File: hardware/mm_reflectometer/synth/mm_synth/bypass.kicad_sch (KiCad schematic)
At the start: 5 parts

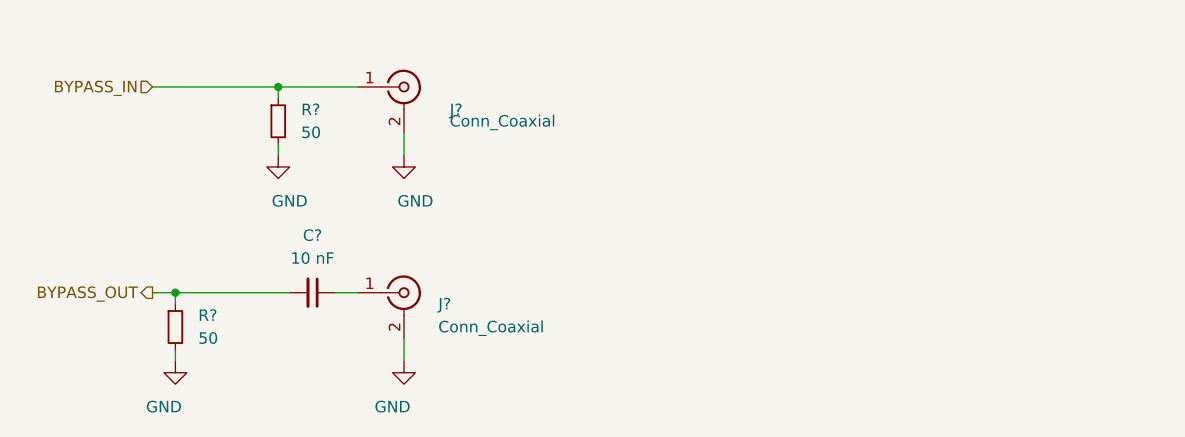
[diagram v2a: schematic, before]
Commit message: work on mm synth schematic - control signals and footprint assignments
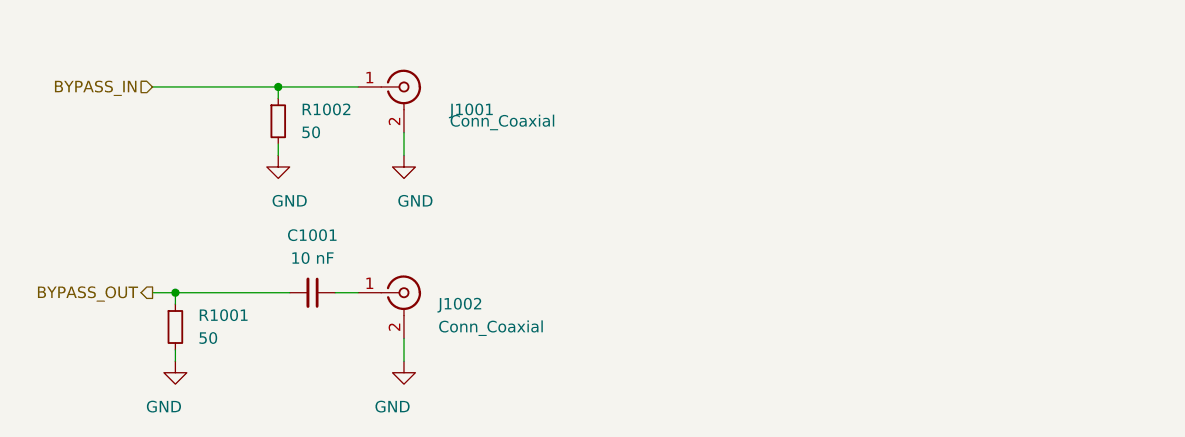
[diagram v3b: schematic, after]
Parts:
- C1001: renamed from C?; footprint (none) -> Capacitor_SMD:C_0402_1005Metric
- J1001, J1002: renamed from J?; footprint (none) -> jtk_rf_footprints:sw_edge_oshpark_4layer
- R1001, R1002: renamed from R?; footprint (none) -> Resistor_SMD:R_0402_1005Metric
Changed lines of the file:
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@@
-(kicad_sch (version 20210406) (generator eeschema)
+(kicad_sch (version 20210621) (generator eeschema)
   (paper "A4")
   (junction (at 110.49 114.3) (diameter 0.9144) (color 0 0 0 0))
@@
   (symbol (lib_id "power:GND") (at 110.49 121.92 0) (mirror y) (unit 1)
     (in_bom yes) (on_board yes)
-    (property "Reference" "#PWR0276" (id 0) (at 110.49 128.27 0)
+    (property "Reference" "#PWR01001" (id 0) (at 110.49 128.27 0)
       (effects (font (size 1.27 1.27)) hide)
     )
@@
   (symbol (lib_id "power:GND") (at 121.92 99.06 0) (unit 1)
     (in_bom yes) (on_board yes)
-    (property "Reference" "#PWR0277" (id 0) (at 121.92 105.41 0)
+    (property "Reference" "#PWR01002" (id 0) (at 121.92 105.41 0)
       (effects (font (size 1.27 1.27)) hide)
     )
@@
   (symbol (lib_id "power:GND") (at 135.89 99.06 0) (unit 1)
     (in_bom yes) (on_board yes)
-    (property "Reference" "#PWR0278" (id 0) (at 135.89 105.41 0)
+    (property "Reference" "#PWR01003" (id 0) (at 135.89 105.41 0)
       (effects (font (size 1.27 1.27)) hide)
     )
@@
   (symbol (lib_id "power:GND") (at 135.89 121.92 0) (mirror y) (unit 1)
     (in_bom yes) (on_board yes)
-    (property "Reference" "#PWR0279" (id 0) (at 135.89 128.27 0)
+    (property "Reference" "#PWR01004" (id 0) (at 135.89 128.27 0)
       (effects (font (size 1.27 1.27)) hide)
     )
@@
   (symbol (lib_id "Device:R_Small") (at 110.49 118.11 0) (unit 1)
     (in_bom yes) (on_board yes)
-    (property "Reference" "R?" (id 0) (at 113.03 116.84 0)
+    (property "Reference" "R1001" (id 0) (at 113.03 116.84 0)
       (effects (font (size 1.27 1.27)) (justify left))
     )
@@
       (effects (font (size 1.27 1.27)) (justify left))
     )
-    (property "Footprint" "" (id 2) (at 110.49 118.11 0)
+    (property "Footprint" "Resistor_SMD:R_0402_1005Metric" (id 2) (at 110.49 118.11 0)
       (effects (font (size 1.27 1.27)) hide)
     )
@@
   (symbol (lib_id "Device:R_Small") (at 121.92 95.25 0) (unit 1)
     (in_bom yes) (on_board yes)
-    (property "Reference" "R?" (id 0) (at 124.46 93.98 0)
+    (property "Reference" "R1002" (id 0) (at 124.46 93.98 0)
       (effects (font (size 1.27 1.27)) (justify left))
     )
@@
       (effects (font (size 1.27 1.27)) (justify left))
     )
-    (property "Footprint" "" (id 2) (at 121.92 95.25 0)
+    (property "Footprint" "Resistor_SMD:R_0402_1005Metric" (id 2) (at 121.92 95.25 0)
       (effects (font (size 1.27 1.27)) hide)
     )
@@
   (symbol (lib_id "Device:C_Small") (at 125.73 114.3 270) (unit 1)
     (in_bom yes) (on_board yes)
-    (property "Reference" "C?" (id 0) (at 125.73 107.95 90))
+    (property "Reference" "C1001" (id 0) (at 125.73 107.95 90))
     (property "Value" "10 nF" (id 1) (at 125.73 110.49 90))
-    (property "Footprint" "" (id 2) (at 125.73 114.3 0)
+    (property "Footprint" "Capacitor_SMD:C_0402_1005Metric" (id 2) (at 125.73 114.3 0)
       (effects (font (size 1.27 1.27)) hide)
     )
@@
   (symbol (lib_id "Connector:Conn_Coaxial") (at 135.89 91.44 0) (unit 1)
     (in_bom yes) (on_board yes)
-    (property "Reference" "J?" (id 0) (at 140.97 93.98 0)
+    (property "Reference" "J1001" (id 0) (at 140.97 93.98 0)
       (effects (font (size 1.27 1.27)) (justify left))
     )
@@
       (effects (font (size 1.27 1.27)) (justify left))
     )
-    (property "Footprint" "" (id 2) (at 135.89 91.44 0)
+    (property "Footprint" "jtk_rf_footprints:sw_edge_oshpark_4layer" (id 2) (at 135.89 91.44 0)
       (effects (font (size 1.27 1.27)) hide)
     )
@@
   (symbol (lib_id "Connector:Conn_Coaxial") (at 135.89 114.3 0) (unit 1)
     (in_bom yes) (on_board yes)
-    (property "Reference" "J?" (id 0) (at 139.7 115.57 0)
+    (property "Reference" "J1002" (id 0) (at 139.7 115.57 0)
       (effects (font (size 1.27 1.27)) (justify left))
     )
@@
       (effects (font (size 1.27 1.27)) (justify left))
     )
-    (property "Footprint" "" (id 2) (at 135.89 114.3 0)
+    (property "Footprint" "jtk_rf_footprints:sw_edge_oshpark_4layer" (id 2) (at 135.89 114.3 0)
       (effects (font (size 1.27 1.27)) hide)
     )

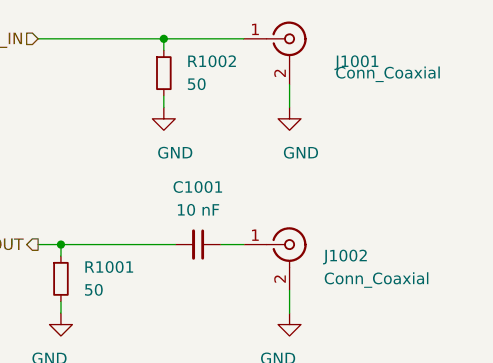
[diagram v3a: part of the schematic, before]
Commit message: created HUSB238 eval board, added clock splitter to mm synth
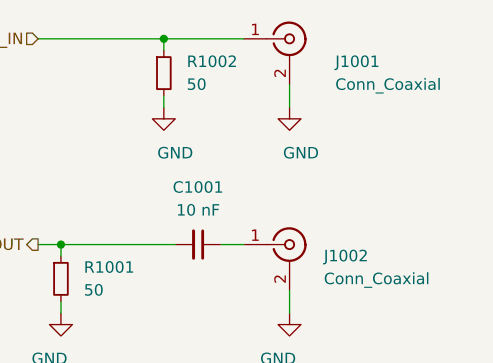
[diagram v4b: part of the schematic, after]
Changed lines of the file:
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@@
       (effects (font (size 1.27 1.27)) (justify left))
     )
-    (property "Value" "Conn_Coaxial" (id 1) (at 140.97 95.25 0)
+    (property "Value" "Conn_Coaxial" (id 1) (at 140.97 96.52 0)
       (effects (font (size 1.27 1.27)) (justify left))
     )

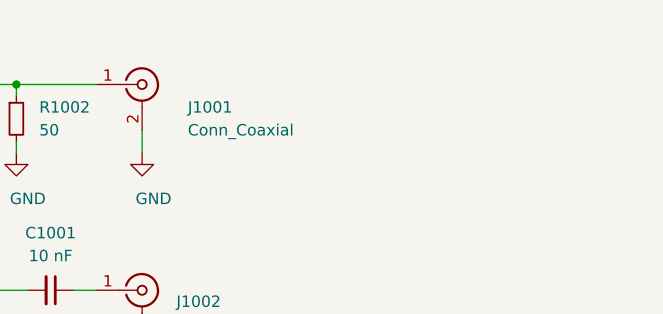
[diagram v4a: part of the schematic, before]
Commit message: component placement on mm synth
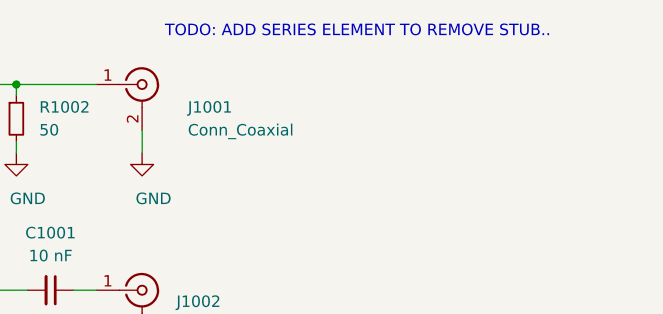
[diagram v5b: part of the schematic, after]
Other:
- note added: "TODO: ADD SERIES ELEMENT TO REMOVE STUB.."
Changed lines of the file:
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@@
     (stroke (width 0) (type solid) (color 0 0 0 0))
+  )
+  (text "TODO: ADD SERIES ELEMENT TO REMOVE STUB.." (at 138.43 86.36 0)
+    (effects (font (size 1.27 1.27)) (justify left bottom))
   )
   (hierarchical_label "BYPASS_IN" (shape input) (at 107.95 91.44 180)

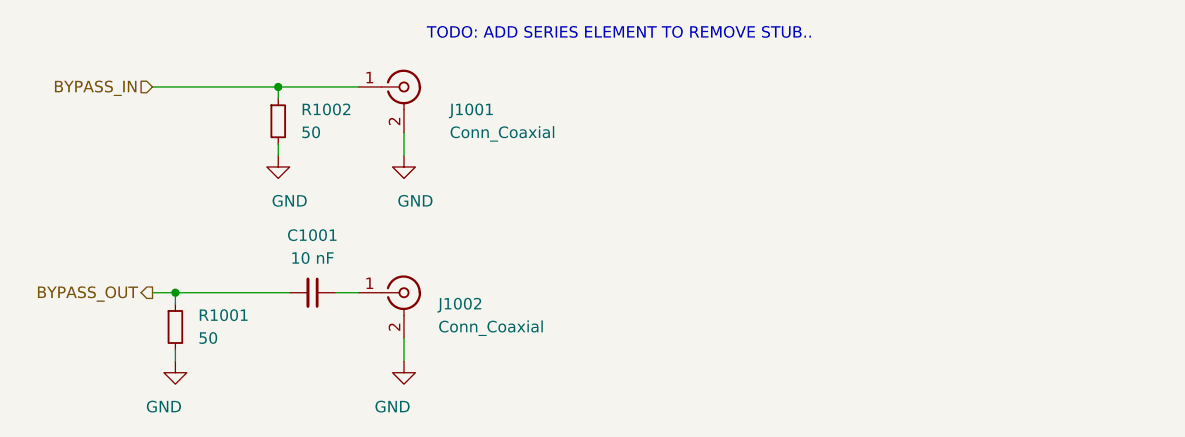
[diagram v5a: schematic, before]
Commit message: more component placement on mm synth
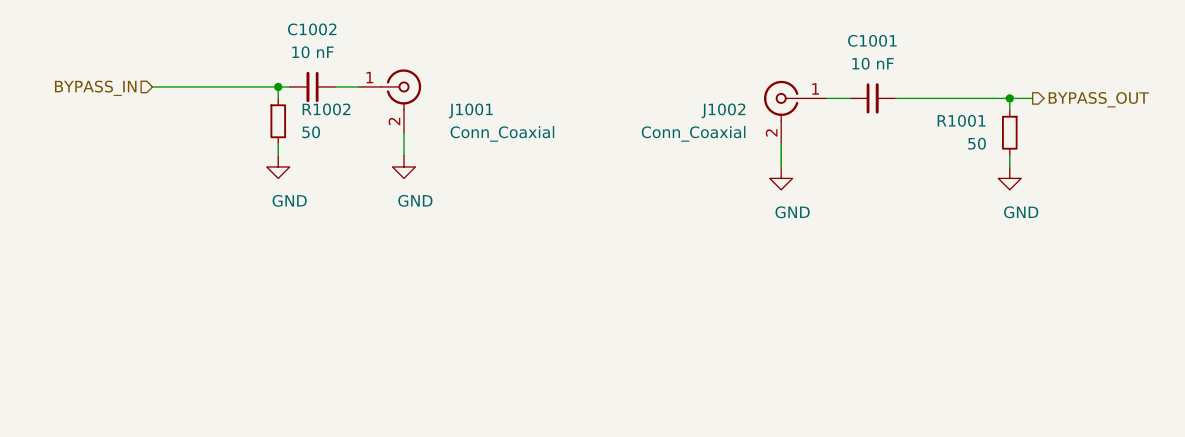
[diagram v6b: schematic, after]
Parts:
- added C1002: 10 nF, Capacitor_SMD:C_0402_1005Metric, symbol Device:C_Small
- J1001, J1002: footprint jtk_rf_footprints:sw_edge_oshpark_4layer -> vna_mm:SF2921-61345
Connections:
- net BYPASS_IN: now also C1002.2; no longer J1001.1 (In)
- new net: C1002.1, J1001.1 (In)
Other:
- note removed: "TODO: ADD SERIES ELEMENT TO REMOVE STUB.."
- moved on the sheet: C1001, J1002, R1001
